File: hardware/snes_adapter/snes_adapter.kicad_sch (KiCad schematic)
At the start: 4 parts, among them J1 CART SLOT TOP ROW, J2 CART SLOT BOTTOM ROW, J3 SNES_Slot

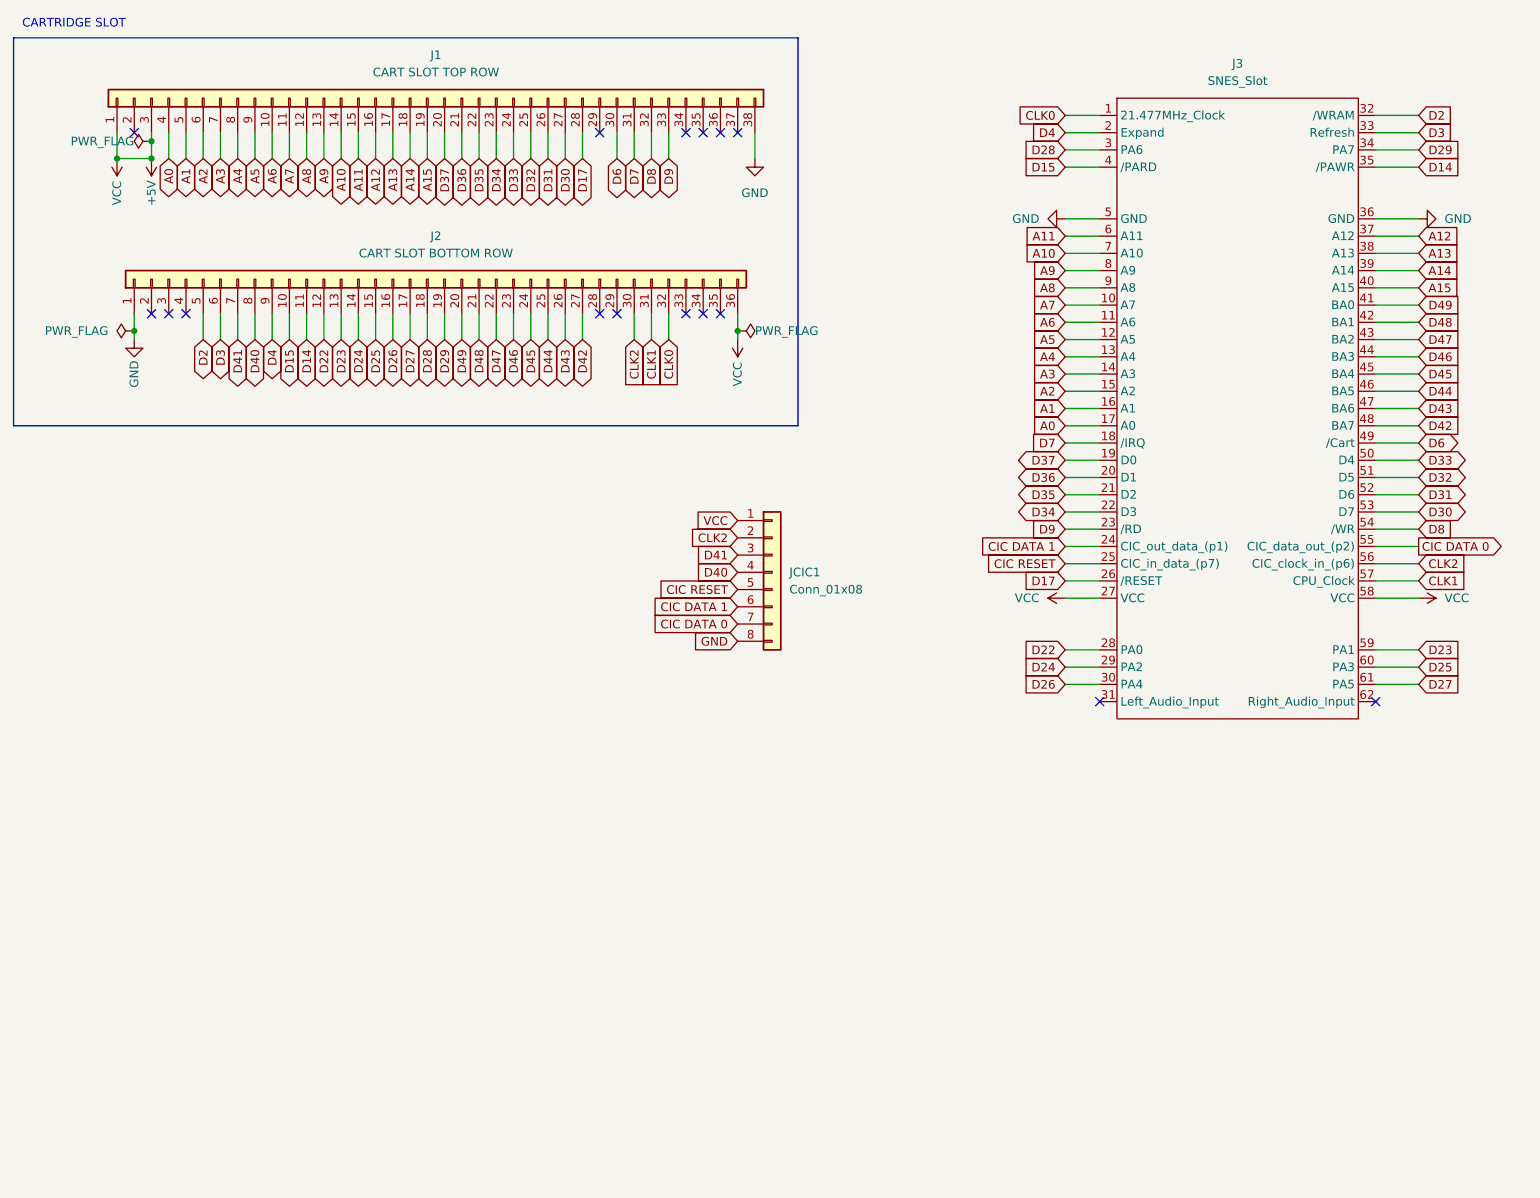
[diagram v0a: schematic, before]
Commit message: update snes breakout
propagate changes in main pcb to snes breakout
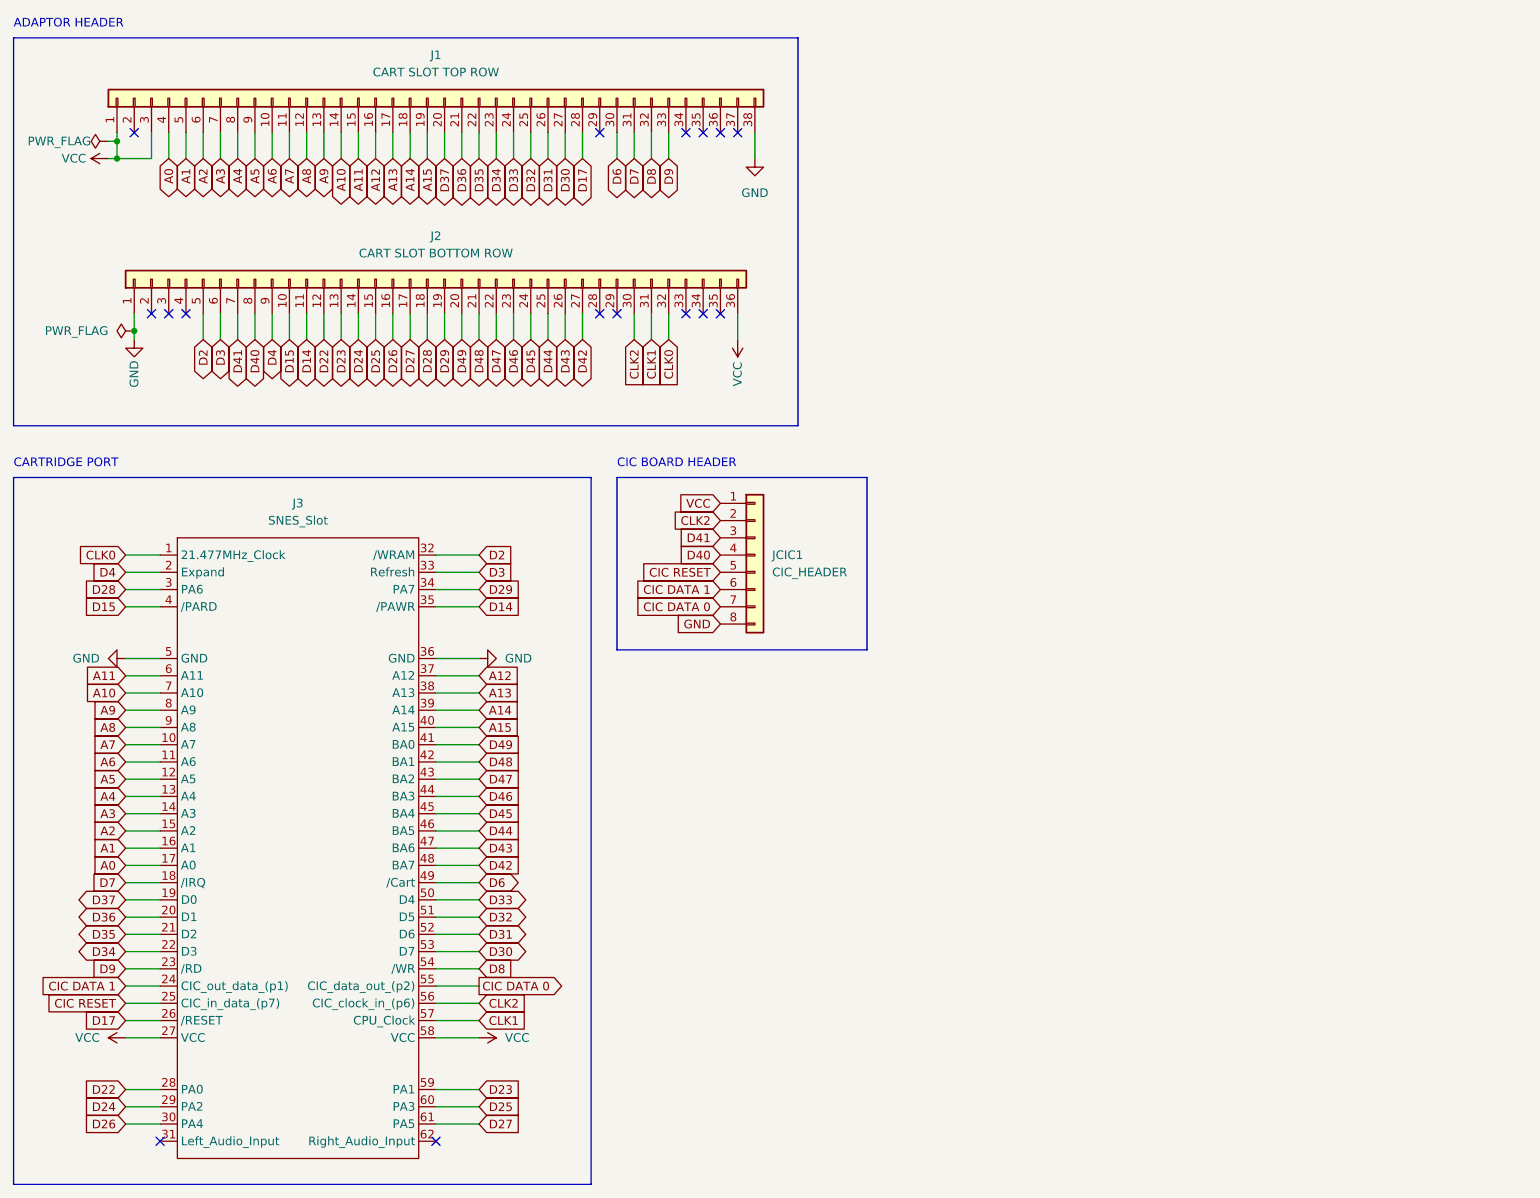
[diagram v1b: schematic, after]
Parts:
- J3: footprint (none) -> !OSCR:SNES Slot; symbol sanni:SNES_Slot -> !OSCR:SNES_Slot
- JCIC1: value Conn_01x08 -> CIC_HEADER; footprint (none) -> Connector_PinHeader_2.54mm:PinHeader_1x08_P2.54mm_Vertical
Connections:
- net +5V renamed VCC
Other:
- note added: "ADAPTOR HEADER"
- note added: "CARTRIDGE PORT"
- note added: "CIC BOARD HEADER"
- note removed: "CARTRIDGE SLOT"
- title: OSCR SNES ADAPTER -> OSCR SHIELD - SNES BREAKOUT
- moved on the sheet: J3, JCIC1

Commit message: wip; down sizing and re-routing traces
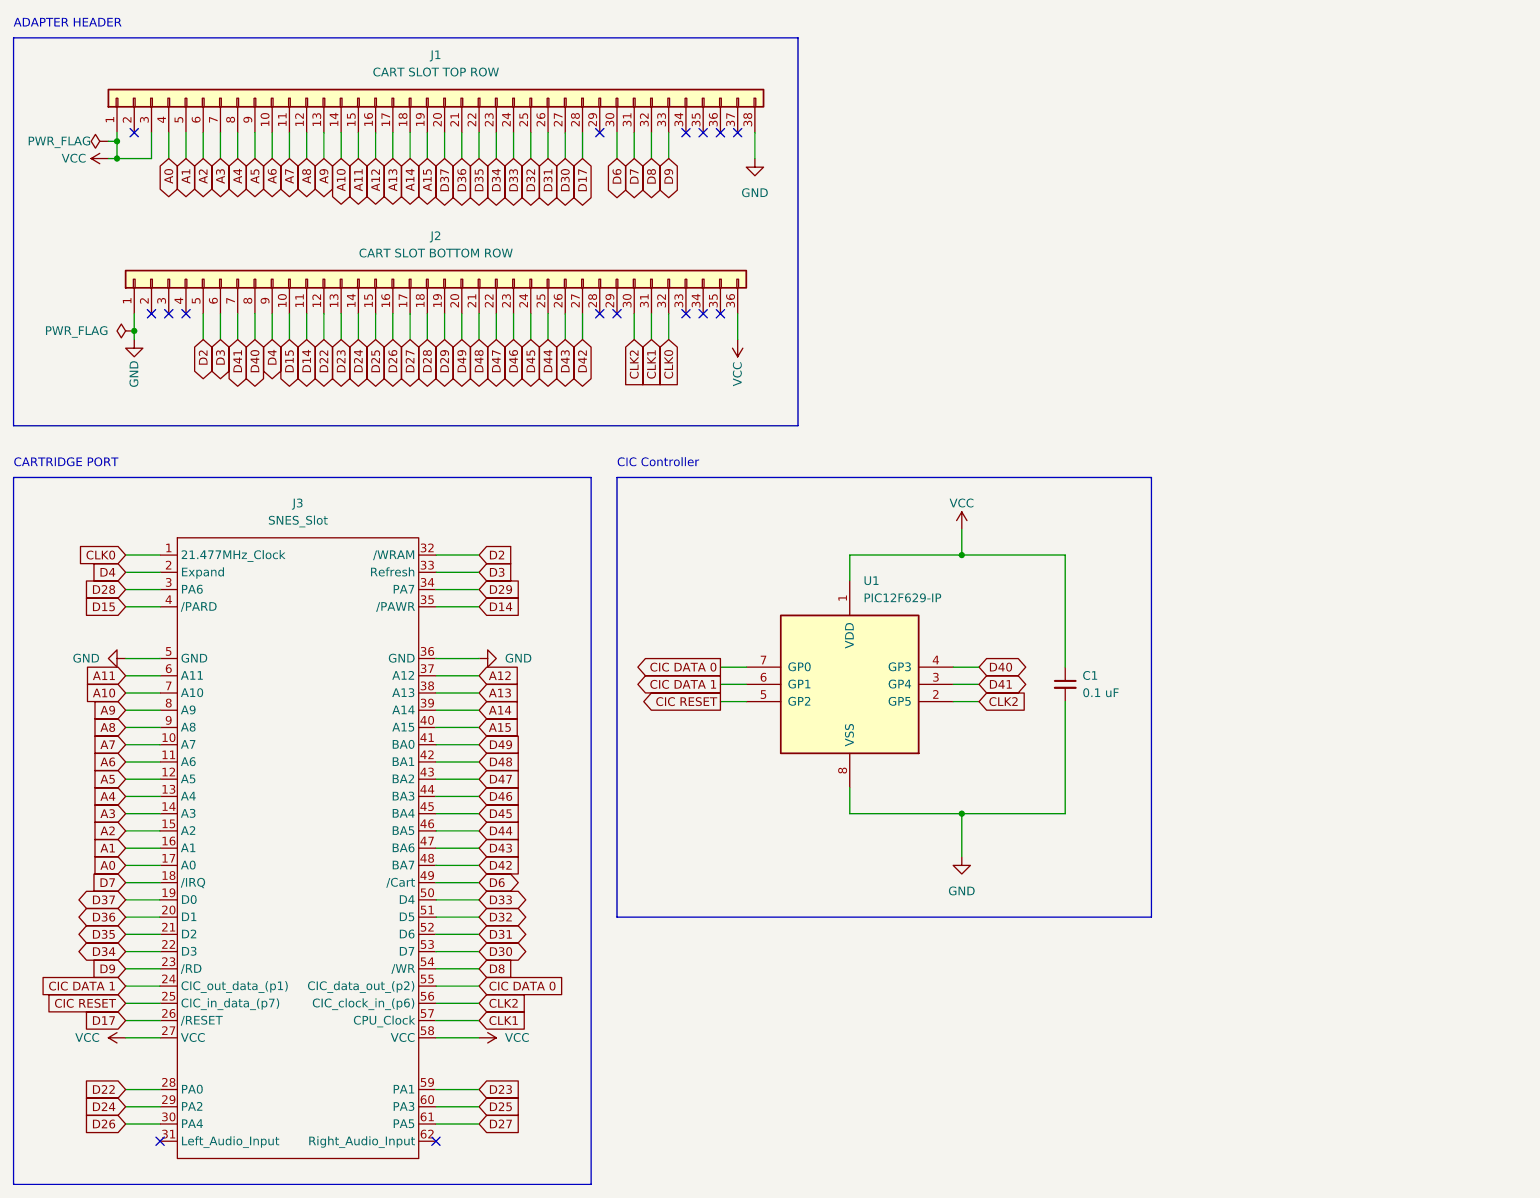
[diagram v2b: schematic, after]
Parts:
- removed JCIC1: CIC_HEADER, Connector_PinHeader_2.54mm:PinHeader_1x08_P2.54mm_Vertical, symbol Connector_Generic:Conn_01x08
- added C1: 0.1 uF, Capacitor_THT:C_Disc_D5.0mm_W2.5mm_P5.00mm, symbol Device:C_Small
- added U1: PIC12F629-IP, Package_DIP:DIP-8_W7.62mm, symbol MCU_Microchip_PIC12:PIC12F629-IP
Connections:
- net CIC DATA 0: now also U1.7 (GP0)
- net CIC DATA 1: now also U1.6 (GP1)
- net CIC RESET: now also U1.5 (GP2)
- net CLK2: now also U1.2 (GP5)
- net D40: now also U1.4 (GP3)
- net D41: now also U1.3 (GP4)
- net GND: now also C1.2, U1.8 (VSS)
- net VCC: now also C1.1, U1.1 (VDD)
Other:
- note added: "ADAPTER HEADER"
- note added: "CIC Controller"
- note removed: "ADAPTOR HEADER"
- note removed: "CIC BOARD HEADER"

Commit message: Move cic uc to SNES breakout board and update
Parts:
- J1: footprint Connector_PinSocket_2.54mm:PinSocket_1x38_P2.54mm_Vertical -> Connector_PinHeader_2.54mm:PinHeader_1x38_P2.54mm_Vertical
- J2: footprint Connector_PinSocket_2.54mm:PinSocket_1x36_P2.54mm_Vertical -> Connector_PinHeader_2.54mm:PinHeader_1x36_P2.54mm_Vertical
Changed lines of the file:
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@@
   (title_block
     (title "OSCR SHIELD - SNES BREAKOUT")
-    (date "2023-01-23")
+    (date "2023-02-10")
   )
   (junction (at 162.56 100.33) (diameter 0) (color 0 0 0 0)
@@
     (property "Reference" "J2" (id 0) (at 85.09 53.34 90))
     (property "Value" "CART SLOT BOTTOM ROW" (id 1) (at 85.09 55.88 90))
-    (property "Footprint" "Connector_PinSocket_2.54mm:PinSocket_1x36_P2.54mm_Vertical" (id 2) (at 83.82 59.69 0)
+    (property "Footprint" "Connector_PinHeader_2.54mm:PinHeader_1x36_P2.54mm_Vertical" (id 2) (at 83.82 59.69 0)
       (effects (font (size 1.27 1.27)) hide)
     )
@@
     (property "Reference" "J1" (id 0) (at 85.09 26.67 90))
     (property "Value" "CART SLOT TOP ROW" (id 1) (at 85.09 29.21 90))
-    (property "Footprint" "Connector_PinSocket_2.54mm:PinSocket_1x38_P2.54mm_Vertical" (id 2) (at 83.82 33.02 0)
+    (property "Footprint" "Connector_PinHeader_2.54mm:PinHeader_1x38_P2.54mm_Vertical" (id 2) (at 83.82 33.02 0)
       (effects (font (size 1.27 1.27)) hide)
     )
@@
     )
     (path "/7f6cd577-ef9e-42a4-adf6-7998d45df605"
-      (reference "J1") (unit 1) (value "CART SLOT TOP ROW") (footprint "Connector_PinSocket_2.54mm:PinSocket_1x38_P2.54mm_Vertical")
+      (reference "J1") (unit 1) (value "CART SLOT TOP ROW") (footprint "Connector_PinHeader_2.54mm:PinHeader_1x38_P2.54mm_Vertical")
     )
     (path "/0137a031-e449-4cf2-a1d4-2cc5020b65f3"
-      (reference "J2") (unit 1) (value "CART SLOT BOTTOM ROW") (footprint "Connector_PinSocket_2.54mm:PinSocket_1x36_P2.54mm_Vertical")
+      (reference "J2") (unit 1) (value "CART SLOT BOTTOM ROW") (footprint "Connector_PinHeader_2.54mm:PinHeader_1x36_P2.54mm_Vertical")
     )
     (path "/280c5ddc-de79-4105-827a-7cfba569bb1b"
